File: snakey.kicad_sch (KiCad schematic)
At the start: 1 part

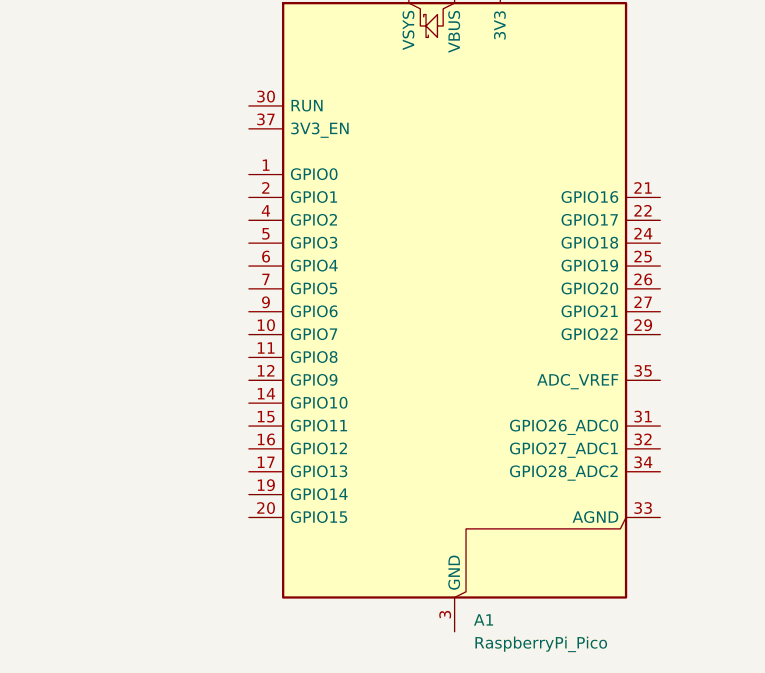
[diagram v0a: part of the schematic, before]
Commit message: mostly done schematic
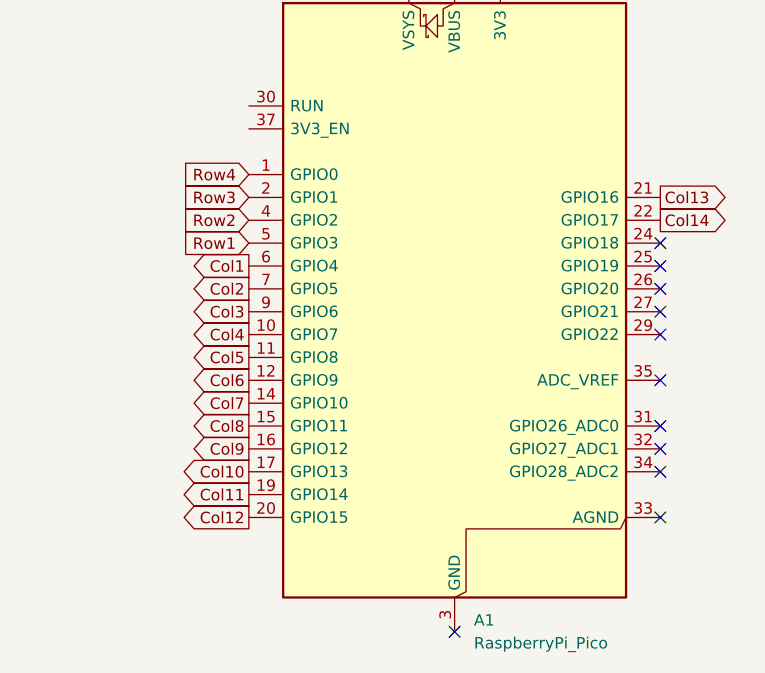
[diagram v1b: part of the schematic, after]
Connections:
- net Row4: now reaches A1.1 (GPIO0)
- net Col4: now reaches A1.10 (GPIO7)
- net Col5: now reaches A1.11 (GPIO8)
- net Col6: now reaches A1.12 (GPIO9)
- net Col7: now reaches A1.14 (GPIO10)
- net Col8: now reaches A1.15 (GPIO11)
- net Col9: now reaches A1.16 (GPIO12)
- net Col10: now reaches A1.17 (GPIO13)
- net Col11: now reaches A1.19 (GPIO14)
- net Row3: now reaches A1.2 (GPIO1)
- net Col12: now reaches A1.20 (GPIO15)
- net Col13: now reaches A1.21 (GPIO16)
- net Col14: now reaches A1.22 (GPIO17)
- net Row2: now reaches A1.4 (GPIO2)
- net Row1: now reaches A1.5 (GPIO3)
- net Col1: now reaches A1.6 (GPIO4)
- net Col2: now reaches A1.7 (GPIO5)
- net Col3: now reaches A1.9 (GPIO6)
- no-connect marks 0 -> 11
